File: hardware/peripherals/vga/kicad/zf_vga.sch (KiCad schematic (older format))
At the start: 3 parts

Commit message: Generate test pattern
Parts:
- removed U? (x2): 74HC590, symbol 74xx:74HC590
- added U? (x2): GAL16V8, symbol Logic_Programmable:GAL16V8
- added U? (x4): 74HC590, symbol 74xx:74HC590
- added U? (x6): 7404, symbol 74xx_IEEE:7404
- added U?: 74HC04, symbol 74xx:74HC04
- added U?: 74HC165, symbol 74xx:74HC165
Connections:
- net GND: now also U?.10 (DS), U?.10 (GND), U?.10 (GND), U?.11 (I10/~OE~), U?.12 (~CE), U?.12 (~CE), U?.14 (~OE), U?.14 (~OE), U?.14 (~OE), U?.14 (~OE), U?.15 (~CE), U?.7 (GND), U?.8 (GND), U?.8 (GND), U?.8 (GND), U?.8 (GND), U?.8 (GND)
- net VCC: now also U?.14 (VCC), U?.16 (VCC), U?.16 (VCC), U?.16 (VCC), U?.16 (VCC), U?.16 (VCC), U?.20 (VCC), U?.20 (VCC)
- net PIXEL_CLOCK renamed CLOCK
- net CLOCK: now also U?.11 (CPC), U?.11 (CPC), U?.13 (CPR), U?.13 (CPR)
- new net: U?.12 (~CE), U?.9 (~RCO) (x2)
- new net #HSYNC: U?.18 (IO2)
- new net #LOAD: U?.1 (~PL), U?.16 (IO4)
- new net #LRESET: U?.10 (~MRC), U?.10 (~MRC), U?.19 (IO1)
- new net #PRESET: U?.1, U?.10 (~MRC), U?.10 (~MRC), U?.19 (IO1)
- new net #VSYNC: U?.18 (IO2)
- new net Gnd: U?.14 (Vcc), U?.14 (Vcc), U?.14 (Vcc), U?.14 (Vcc), U?.14 (Vcc), U?.14 (Vcc), U?.7 (Gnd), U?.7 (Gnd), U?.7 (Gnd), U?.7 (Gnd), U?.7 (Gnd), U?.7 (Gnd)
- new net HSTICK: U?.1 (I1/CLK), U?.17 (I03)
- new net L0: U?.1 (I1/CLK), U?.15 (Q0)
- new net L1: U?.1 (Q1), U?.2 (I2)
- new net L2: U?.2 (Q2), U?.3 (I3)
- new net L3: U?.3 (Q3), U?.4 (I4)
- new net L4: U?.4 (Q4), U?.5 (I5)
- new net L5: U?.5 (Q5), U?.6 (I6)
- new net L6: U?.6 (Q6), U?.7 (I7)
- new net L7: U?.7 (Q7), U?.8 (I8)
- new net L8: U?.15 (Q0), U?.9 (I9)
- new net L9: U?.1 (Q1), U?.11 (I10/~OE~)
- new net P0: U?.15 (Q0), U?.2 (I2)
- new net P1: U?.1 (Q1), U?.3, U?.3 (I3)
- new net P2: U?.2 (Q2), U?.4 (I4)
- new net P3: U?.3 (Q3), U?.5 (I5)
- new net P4: U?.4 (Q4), U?.6 (I6)
- new net P5: U?.5 (Q5), U?.7 (I7)
- new net P6: U?.6 (Q6), U?.8 (I8)
- new net P7: U?.7 (Q7), U?.9 (I9)
- new net P8: U?.12 (IO8), U?.15 (Q0)
- new net P9: U?.1 (Q1), U?.13 (IO7)
- new net PRESET: U?.11 (CPC), U?.11 (CPC), U?.13 (CPR), U?.13 (CPR), U?.2
- new net SERIAL: U?.9 (Q7)
- new net SHIFT: U?.2 (CP), U?.4
- no-connect marks 1 -> 13
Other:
- note added: "Horizontal Decoder"
- note added: "Line Counter"
- note added: "Pixel Counter"
- note added: "Vertical Decoder"
- moved on the sheet: X?

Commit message: Update zf_vga.sch
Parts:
- added U? (x2): 74HC590, symbol 74xx:74HC590
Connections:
- net #LRESET: now also U?.10 (~MRC)
- net GND: now also U?.8 (GND), U?.8 (GND)
- net L1: now also U?.11
- net P4: now also U?.9
- net VCC: now also U?.16 (VCC), U?.16 (VCC)
- net ALRESET: now reaches U?.5
- net ALRESET: now also U?.4 (Q4)
- net #ALRESET: now reaches U?.6
- net #ALRESET: now also U?.10 (~MRC)
- net #P4: now reaches U?.8
- net #P4: now also U?.11 (CPC), U?.13 (CPR)
- net #L1: now reaches U?.10
- net #L1: now also U?.11 (CPC), U?.13 (CPR)
- new net A0: U?.15 (Q0)
- new net A1: U?.1 (Q1)
- new net A2: U?.2 (Q2)
- new net A3: U?.3 (Q3)
- new net A4: U?.15 (Q0)
- new net A5: U?.1 (Q1)
- new net A6: U?.2 (Q2)
- new net A7: U?.3 (Q3)
- new net A8: U?.4 (Q4)
- new net A9: U?.5 (Q5)
- no-connect marks 13 -> 18
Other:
- note added: "Lower Address Counter"
- note added: "Upper Address Counter"
- note added: "Video Output"
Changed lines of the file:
@@
 $EndDescr
-$Comp
-L 74xx:74HC165 U?
-U 1 1 622A653B
-P 6850 1650
-F 0 "U?" H 6850 2731 50  0000 C CNN
-F 1 "74HC165" H 6850 2640 50  0000 C CNN
-F 2 "" H 6850 1650 50  0001 C CNN
-F 3 "https://assets.nexperia.com/documents/data-sheet/74HC_HCT165.pdf" H 6850 1650 50  0001 C CNN
-	1    6850 1650
-	1    0    0    -1
-$EndComp
 $Comp
 L power:GND #PWR0124
@@
 Wire Wire Line
 	6350 2650 6350 2350
-Connection ~ 6850 2650
 Text GLabel 1850 1050 2    50   Input ~ 0
 P0
@@
 Wire Wire Line
 	1050 3850 1450 3850
-Text GLabel 1050 3250 0    50   Input ~ 0
-#LRESET
 Wire Wire Line
 	1050 2950 1050 3000
@@
 Text GLabel 5550 1700 2    50   Input ~ 0
 SHIFT
+$Comp
+L 74xx:74HC590 U?
+U 1 1 62199935
+P 8550 1550
+F 0 "U?" H 8550 2431 50  0000 C CNN
+F 1 "74HC590" H 8550 2340 50  0000 C CNN
+F 2 "" H 8550 1600 50  0001 C CNN
+F 3 "https://assets.nexperia.com/documents/data-sheet/74HC590.pdf" H 8550 1600 50  0001 C CNN
+	1    8550 1550
+	1    0    0    -1
+$EndComp
+Wire Wire Line
+	8800 850  8550 850
+$Comp
+L power:VCC #PWR?
+U 1 1 6219AD3B
+P 8800 850
+F 0 "#PWR?" H 8800 700 50  0001 C CNN
+F 1 "VCC" H 8815 1023 50  0000 C CNN
+F 2 "" H 8800 850 50  0001 C CNN
+F 3 "" H 8800 850 50  0001 C CNN
+	1    8800 850
+	1    0    0    -1
+$EndComp
+$Comp
+L 74xx:74HC590 U?
+U 1 1 6219DA0D
+P 10250 1550
+F 0 "U?" H 10250 2431 50  0000 C CNN
+F 1 "74HC590" H 10250 2340 50  0000 C CNN
+F 2 "" H 10250 1600 50  0001 C CNN
+F 3 "https://assets.nexperia.com/documents/data-sheet/74HC590.pdf" H 10250 1600 50  0001 C CNN
+	1    10250 1550
+	1    0    0    -1
+$EndComp
+Wire Wire Line
+	10500 850  10250 850
+$Comp
+L power:VCC #PWR?
+U 1 1 6219DA14
+P 10500 850
+F 0 "#PWR?" H 10500 700 50  0001 C CNN
+F 1 "VCC" H 10515 1023 50  0000 C CNN
+F 2 "" H 10500 850 50  0001 C CNN
+F 3 "" H 10500 850 50  0001 C CNN
+	1    10500 850
+	1    0    0    -1
+$EndComp
+Text GLabel 8950 1050 2    50   Input ~ 0
+A0
+Text GLabel 8950 1150 2    50   Input ~ 0
+A1
+Text GLabel 8950 1250 2    50   Input ~ 0
+A2
+Text GLabel 8950 1450 2    50   Input ~ 0
+ALRESET
+Text GLabel 4450 2200 0    50   Input ~ 0
+ALRESET
+Text GLabel 5550 2200 2    50   Input ~ 0
+#ALRESET
+Text GLabel 8150 1550 0    50   Input ~ 0
+#ALRESET
+Text GLabel 10650 1050 2    50   Input ~ 0
+A4
+Text GLabel 10650 1150 2    50   Input ~ 0
+A5
+Text GLabel 10650 1250 2    50   Input ~ 0
+A6
+Text GLabel 10650 1350 2    50   Input ~ 0
+A7
+Text GLabel 10650 1450 2    50   Input ~ 0
+A8
+Text GLabel 10650 1550 2    50   Input ~ 0
+A9
+Text GLabel 8950 1350 2    50   Input ~ 0
+A3
+NoConn ~ 10650 1650
+NoConn ~ 10650 1750
+NoConn ~ 8950 1750
+NoConn ~ 8950 1650
+NoConn ~ 8950 1550
+$Comp
+L power:GND #PWR?
+U 1 1 621B7085
+P 8550 2150
+F 0 "#PWR?" H 8550 1900 50  0001 C CNN
+F 1 "GND" H 8555 1977 50  0000 C CNN
+F 2 "" H 8550 2150 50  0001 C CNN
+F 3 "" H 8550 2150 50  0001 C CNN
+	1    8550 2150
+	1    0    0    -1
+$EndComp
+$Comp
+L power:GND #PWR?
+U 1 1 621B7A12
+P 10250 2150
+F 0 "#PWR?" H 10250 1900 50  0001 C CNN
+F 1 "GND" H 10255 1977 50  0000 C CNN
+F 2 "" H 10250 2150 50  0001 C CNN
+F 3 "" H 10250 2150 50  0001 C CNN
+	1    10250 2150
+	1    0    0    -1
+$EndComp
+Wire Wire Line
+	8150 1250 8150 1300
+Wire Wire Line
+	8150 1300 8100 1300
+Connection ~ 8150 1300
+Wire Wire Line
+	8150 1300 8150 1350
+Wire Wire Line
+	9850 1250 9850 1300
+Wire Wire Line
+	9850 1300 9800 1300
+Connection ~ 9850 1300
+Wire Wire Line
+	9850 1300 9850 1350
+Text GLabel 4450 3200 0    50   Input ~ 0
+L1
+Text GLabel 5550 3200 2    50   Input ~ 0
+#L1
+Text GLabel 9800 1300 0    50   Input ~ 0
+#L1
+Text GLabel 4450 2700 0    50   Input ~ 0
+P4
+Text GLabel 5550 2700 2    50   Input ~ 0
+#P4
+Text GLabel 8100 1300 0    50   Input ~ 0
+#P4
+Text Notes 8600 2150 0    50   ~ 0
+Lower Address Counter
+Text Notes 10300 2150 0    50   ~ 0
+Upper Address Counter
+Connection ~ 6850 2650
+Text Notes 6900 2600 0    50   ~ 0
+Video Output
+$Comp
+L 74xx:74HC165 U?
+U 1 1 622A653B
+P 6850 1650
+F 0 "U?" H 6850 2731 50  0000 C CNN
+F 1 "74HC165" H 6850 2640 50  0000 C CNN
+F 2 "" H 6850 1650 50  0001 C CNN
+F 3 "https://assets.nexperia.com/documents/data-sheet/74HC_HCT165.pdf" H 6850 1650 50  0001 C CNN
+	1    6850 1650
+	1    0    0    -1
+$EndComp
+Text GLabel 1050 3250 0    50   Input ~ 0
+#LRESET
+Text GLabel 9850 1550 0    50   Input ~ 0
+#LRESET
 $EndSCHEMATC

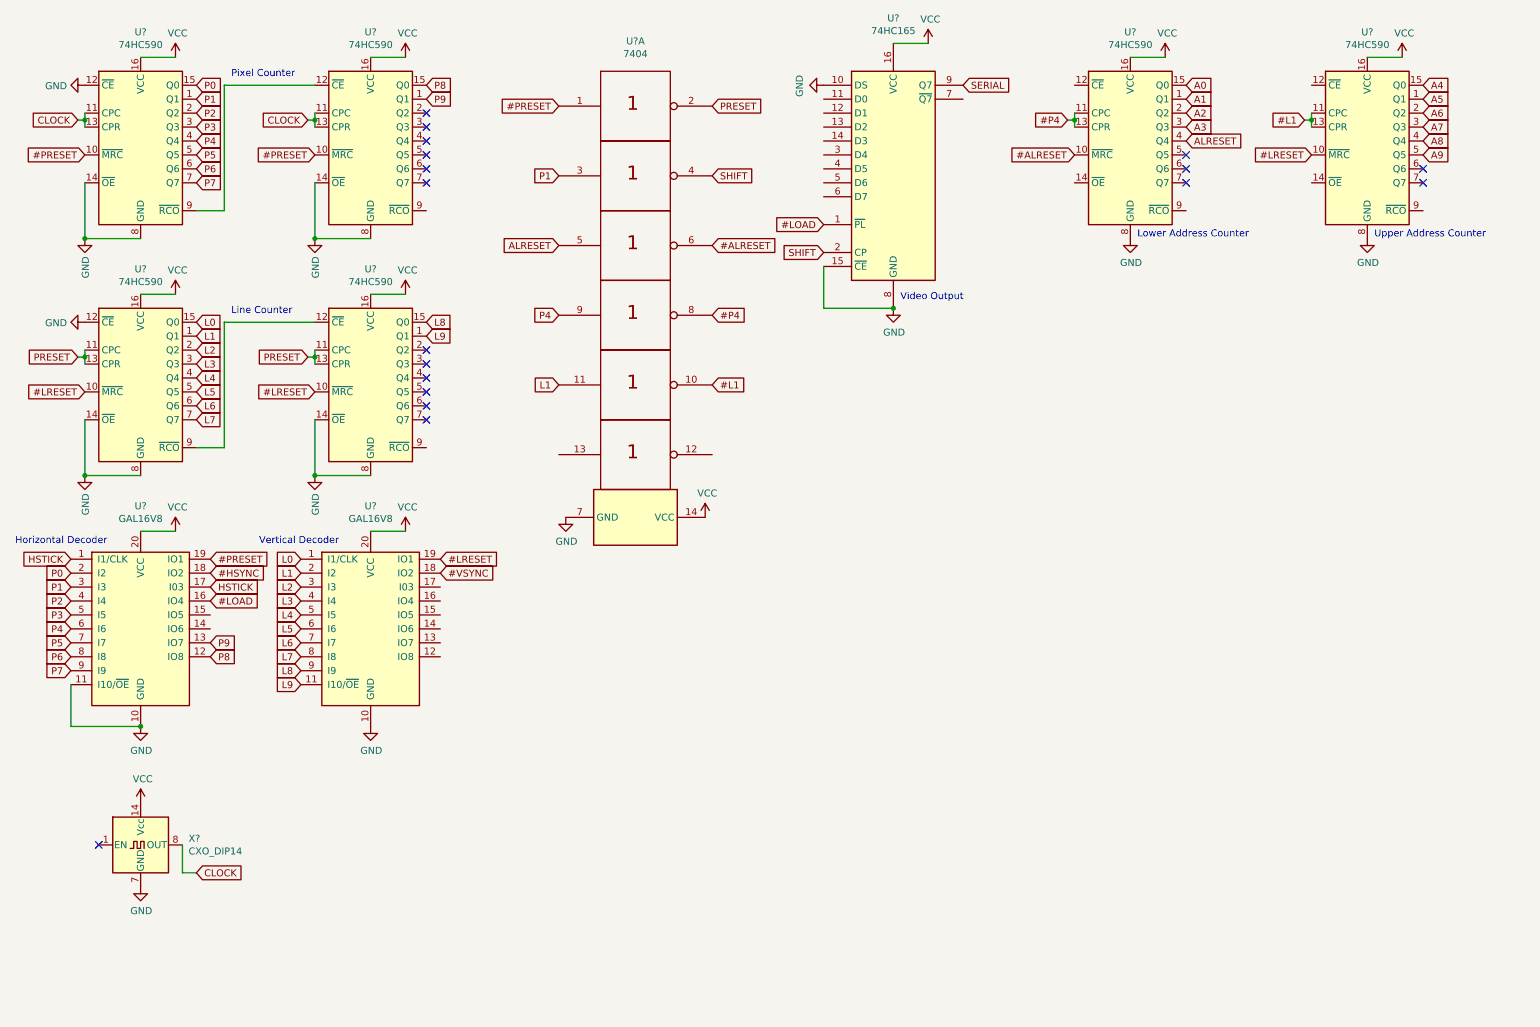
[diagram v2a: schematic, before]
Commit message: Removed address counters
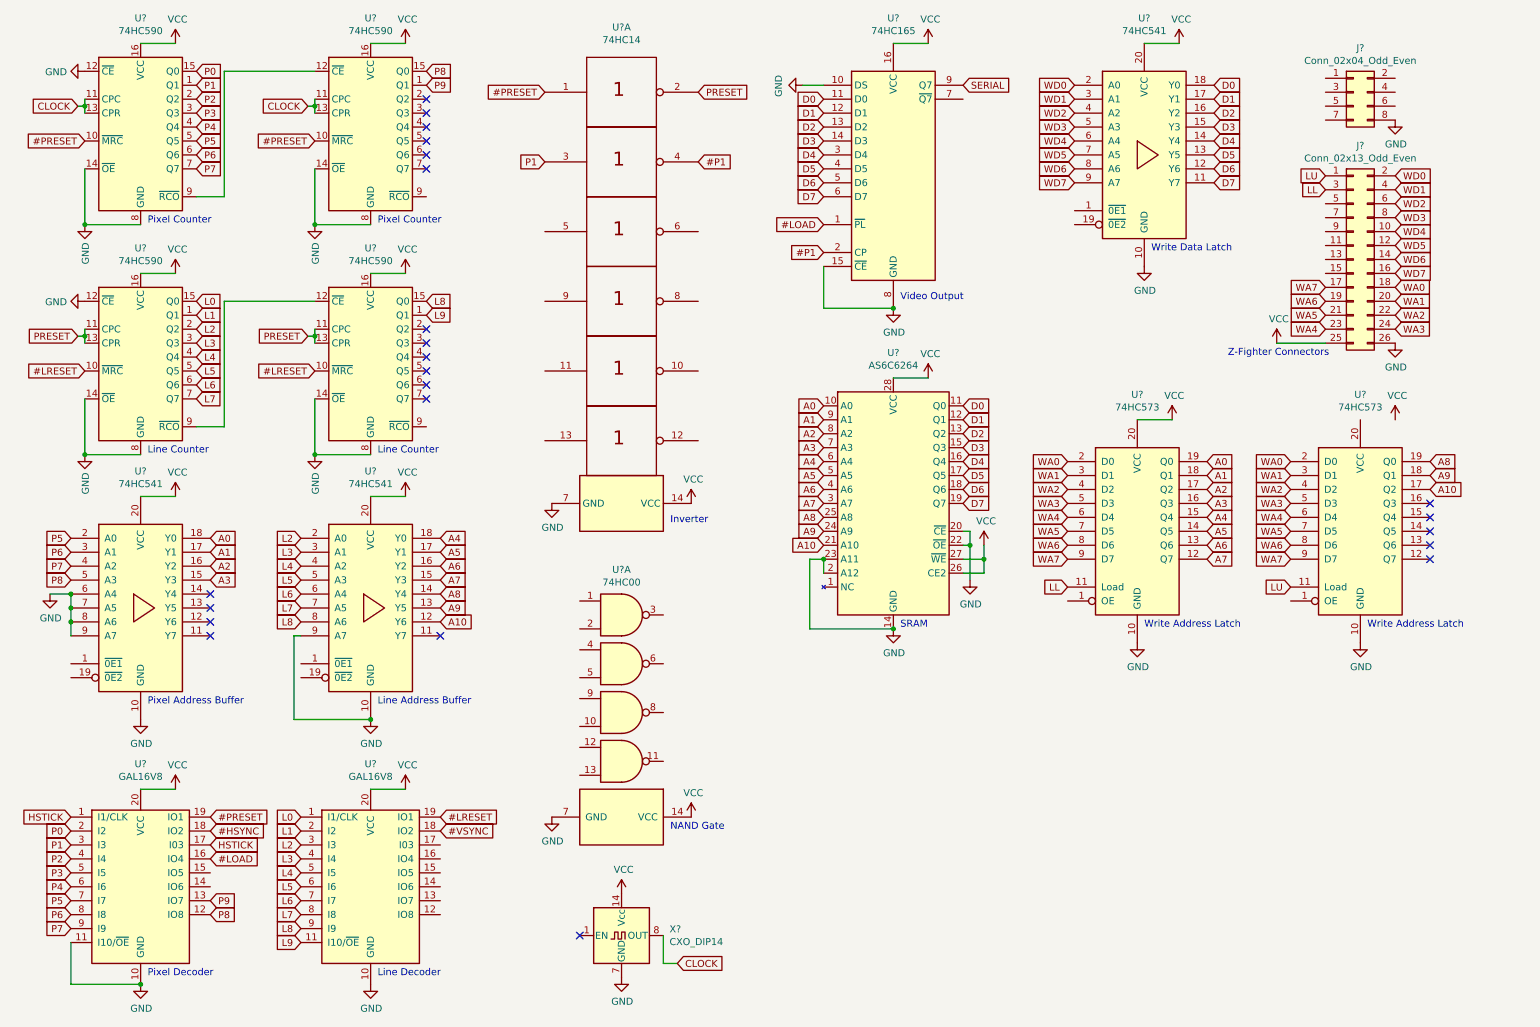
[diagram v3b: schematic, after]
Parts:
- removed U? (x2): 74HC590, symbol 74xx:74HC590
- added J?: Conn_02x13_Odd_Even, symbol Connector_Generic:Conn_02x13_Odd_Even
- added J?: Conn_02x04_Odd_Even, symbol Connector_Generic:Conn_02x04_Odd_Even
- added U? (x3): 74HC541, symbol 74xx:74HC541
- added U? (x2): 74HC573, symbol 74xx:74LS573
- added U? (x5): 74HC00, symbol 74xx:74HC00
- added U?: AS6C6264, Package_DIP:DIP-28_W15.24mm, symbol Memory_RAM:AS6C6264
- U?: value 7404 -> 74HC14
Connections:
- net A0: now also U?.10 (A0), U?.18 (Y0), U?.19 (Q0)
- net A1: now also U?.17 (Y1), U?.18 (Q1), U?.9 (A1)
- net A2: now also U?.16 (Y2), U?.17 (Q2), U?.8 (A2)
- net A3: now also U?.15 (Y3), U?.16 (Q3), U?.7 (A3)
- net A4: now also U?.15 (Q4), U?.18 (Y0), U?.6 (A4)
- net A5: now also U?.14 (Q5), U?.17 (Y1), U?.5 (A5)
- net A6: now also U?.13 (Q6), U?.16 (Y2), U?.4 (A6)
- net A7: now also U?.12 (Q7), U?.15 (Y3), U?.3 (A7)
- net A8: now also U?.14 (Y4), U?.19 (Q0), U?.25 (A8)
- net A9: now also U?.13 (Y5), U?.18 (Q1), U?.24 (A9)
- net GND: now also J?.26 (Pin_26), J?.8 (Pin_8), U?.10 (GND), U?.10 (GND), U?.10 (GND), U?.10 (GND), U?.10 (GND), U?.14 (GND), U?.2 (A12), U?.20 (~CE), U?.22 (~OE), U?.23 (A11), U?.6 (A4), U?.7 (A5), U?.7 (GND), U?.8 (A6), U?.9 (A7), U?.9 (A7)
- net L1: no longer U?.11
- net L2: now also U?.2 (A0)
- net L3: now also U?.3 (A1)
- net L4: now also U?.4 (A2)
- net L5: now also U?.5 (A3)
- net L6: now also U?.6 (A4)
- net L7: now also U?.7 (A5)
- net L8: now also U?.8 (A6)
- net P4: no longer U?.9
- net P5: now also U?.2 (A0)
- net P6: now also U?.3 (A1)
- net P7: now also U?.4 (A2)
- net P8: now also U?.5 (A3)
- net VCC: now also J?.25 (Pin_25), U?.14 (VCC), U?.20 (VCC), U?.20 (VCC), U?.20 (VCC), U?.20 (VCC), U?.26 (CE2), U?.27 (~WE), U?.28 (VCC)
- net D0: now reaches U?.11 (D0)
- net D0: now also U?.11 (Q0), U?.18 (Y0)
- net D1: now reaches U?.12 (D1)
- net D1: now also U?.12 (Q1), U?.17 (Y1)
- net D2: now reaches U?.13 (D2)
- net D2: now also U?.13 (Q2), U?.16 (Y2)
- net D3: now reaches U?.14 (D3)
- net D3: now also U?.15 (Q3), U?.15 (Y3)
- net D4: now reaches U?.3 (D4)
- net D4: now also U?.14 (Y4), U?.16 (Q4)
- net D5: now reaches U?.4 (D5)
- net D5: now also U?.13 (Y5), U?.17 (Q5)
- net D6: now reaches U?.5 (D6)
- net D6: now also U?.12 (Y6), U?.18 (Q6)
- net D7: now reaches U?.6 (D7)
- net D7: now also U?.11 (Y7), U?.19 (Q7)
- net #ALRESET: no longer names the net of U?.6
- net #L1: no longer names the net of U?.10
- net #P4: no longer names the net of U?.8
- net ALRESET: no longer names the net of U?.5
- net SHIFT renamed #P1
- new net A10: U?.12 (Y6), U?.17 (Q2), U?.21 (A10)
- new net LL: J?.3 (Pin_3), U?.11 (Load)
- new net LU: J?.1 (Pin_1), U?.11 (Load)
- new net WA0: J?.18 (Pin_18), U?.2 (D0), U?.2 (D0)
- new net WA1: J?.20 (Pin_20), U?.3 (D1), U?.3 (D1)
- new net WA2: J?.22 (Pin_22), U?.4 (D2), U?.4 (D2)
- new net WA3: J?.24 (Pin_24), U?.5 (D3), U?.5 (D3)
- new net WA4: J?.23 (Pin_23), U?.6 (D4), U?.6 (D4)
- new net WA5: J?.21 (Pin_21), U?.7 (D5), U?.7 (D5)
- new net WA6: J?.19 (Pin_19), U?.8 (D6), U?.8 (D6)
- new net WA7: J?.17 (Pin_17), U?.9 (D7), U?.9 (D7)
- new net WD0: J?.2 (Pin_2), U?.2 (A0)
- new net WD1: J?.4 (Pin_4), U?.3 (A1)
- new net WD2: J?.6 (Pin_6), U?.4 (A2)
- new net WD3: J?.8 (Pin_8), U?.5 (A3)
- new net WD4: J?.10 (Pin_10), U?.6 (A4)
- new net WD5: J?.12 (Pin_12), U?.7 (A5)
- new net WD6: J?.14 (Pin_14), U?.8 (A6)
- new net WD7: J?.16 (Pin_16), U?.9 (A7)
- no-connect marks 18 -> 23
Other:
- note added: "Inverter"
- note added: "Line Address Buffer"
- note added: "Line Decoder"
- note added: "NAND Gate"
- note added: "Pixel Address Buffer"
- note added: "Pixel Decoder"
- note added: "SRAM"
- note added: "Write Address Latch"
- note added: "Write Data Latch"
- note added: "Z-Fighter Connectors"
- note removed: "Horizontal Decoder"
- note removed: "Lower Address Counter"
- note removed: "Upper Address Counter"
- note removed: "Vertical Decoder"
- moved on the sheet: U?, U?A, X?

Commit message: Update zf_vga.sch
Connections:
- net labels added: #WRDY, ACTVID, CC, CD1, CD2, CL
- wire segments 65 -> 77
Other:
- note added: "Write Address Latch (Hi)"
- note added: "Write Address Latch (Lo)"
- note added: "Write Data Buffer"
- note removed: "Write Address Latch"
- note removed: "Write Data Latch"
- moved on the sheet: U?

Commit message: Write circuit
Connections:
- net labels added: #P0, #WE, CE2, HRESET, HSET, LACTIVE
- net labels removed: ACTVID, HSTICK
- wire segments 77 -> 84
- no-connect marks 23 -> 25
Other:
- note added: "#HSYNC latch"
- note added: "CE2 low during address transitions"
- note added: "Read Cycle: /OE low, /CE low, /WE high, CE2 high\nWrite Cycle: /CE low, /WE low, CE2 high\n"WE#, CE# must be high or CE2 must be low\nduring all address transitions.""
- note added: "Valid data on write address latches"
- moved on the sheet: U?, U?A
